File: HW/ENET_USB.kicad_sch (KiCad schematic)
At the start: 0 parts

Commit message: USB hub, connector, load switch
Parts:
- added C? (x2): 100uF, Capacitor_SMD:CP_Elec_6.3x5.8, symbol Device:C_Polarized_US
- added C? (x3): 0.1u, Capacitor_SMD:C_0603_1608Metric, symbol Device:C
- added C? (x3): 22uF, Capacitor_SMD:C_1210_3225Metric, symbol Device:C
- added C? (x2): 1u, Capacitor_SMD:C_0603_1608Metric, symbol Device:C
- added C? (x2): 18pF, Capacitor_SMD:C_0603_1608Metric, symbol Device:C
- added J?: UJ2-ADH-1-TH, symbol KlipperShip_Symbols:UJ2-ADH-1-TH
- added R?: 0R, Resistor_SMD:R_0603_1608Metric, symbol Device:R_US
- added R?: 12k 1%, Resistor_SMD:R_0603_1608Metric, symbol Device:R_US
- added U?: USB2422, Package_DFN_QFN:QFN-24-1EP_4x4mm_P0.5mm_EP2.6x2.6mm, symbol KlipperShip_Symbols:USB2422
- added U?: TPS2042D, Package_SO:SOIC-8_3.9x4.9mm_P1.27mm, symbol Power_Management:TPS2042D
- added Y?: 24MHz, Crystal:Crystal_SMD_3225-4Pin_3.2x2.5mm, symbol Device:Crystal_GND24
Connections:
- new net +3V3: C?.1, C?.1, C?.1, R?.1, U?.1 (VDD33), U?.18 (VDD33), U?.9 (VDD33)
- new net +5V: C?.1, U?.2 (IN1)
- new net GND: C?.2, C?.2, C?.2, C?.2, C?.2, C?.2, C?.2, C?.2, C?.2, C?.2, C?.2, C?.2, J?.4 (GND), J?.8 (GND), R?.2, U?.1 (GND), U?.25 (PAD), Y?.2, Y?.4
- new net I2C_USB_SCL: U?.14 (SCL)
- new net I2C_USB_SDA: U?.13 (SDA)
- new net USB_CM_DN: U?.19 (USB_UP_DM)
- new net USB_CM_DP: U?.20 (USB_UP_DP)
- new net USB_DS1_DM: J?.2 (DM1), U?.2 (USB_DS1_DM)
- new net USB_DS1_DP: J?.3 (DP1), U?.3 (USB_DS1_DP)
- new net USB_DS2_DM: J?.6 (DM2), U?.4 (USB_DS2_DM)
- new net USB_DS2_DP: J?.7 (DP2), U?.5 (USB_DS2_DP)
- new net USB_RBIAS: R?.1, U?.24 (RBIAS)
- new net USB_RST: U?.15 (RST_N)
- new net USB_VBUS_DIV: R?.2, U?.16 (VBUS_DET)
- new net USB_VDD_CAP: C?.1, U?.10 (VDD_CAP)
- new net USB_VDD_PLL: C?.1, U?.23 (VDD_PLL)
- new net USB_XTAL_N: U?.21 (XTALOUT)
- new net USB_XTAL_P: C?.1, U?.22 (XTALIN), Y?.1
- new net UXB_XTAL_N: C?.1, Y?.3
- new net VBUS1: C?.1, C?.1, J?.1 (VCC1), U?.7 (OUT1)
- new net VBUS2: C?.1, C?.1, J?.5 (VCC2), U?.6 (OUT2)
- no-connect marks 0 -> 1
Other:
- note added: "PIN 1"
- note added: "PIN 18"
- note added: "PIN 9"

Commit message: More work on USB, added Enet jack
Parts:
- removed U?: TPS2042D, Package_SO:SOIC-8_3.9x4.9mm_P1.27mm, symbol Power_Management:TPS2042D
- added C? (x2): 0.1u, Capacitor_SMD:C_0603_1608Metric, symbol Device:C
- added J?: RJ45_Amphenol_RJMG1BD3B8K1ANR, Connector_RJ:RJ45_Amphenol_RJMG1BD3B8K1ANR, symbol Connector:RJ45_Amphenol_RJMG1BD3B8K1ANR
- added R? (x3): 0R, Resistor_SMD:R_0603_1608Metric, symbol Device:R_US
- added R? (x4): 10k 1%, Resistor_SMD:R_0603_1608Metric, symbol Device:R_US
- added R? (x2): 100R, Resistor_SMD:R_0603_1608Metric, symbol Device:R_US
- added U?: TPS2052BDR, Package_SO:SOIC-8_3.9x4.9mm_P1.27mm, symbol KlipperShip_Symbols:TPS2052BDR
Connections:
- net +3V3: now also J?.L1 (LEDY_A), J?.L4 (LEDG_A), R?.1, R?.1
- net +5V: now also U?.2 (IN1)
- net GND: now also C?.2, C?.2, J?.R8 (GND), R?.2, R?.2, U?.1 (GND)
- net I2C_USB_SCL: now also R?.2
- net I2C_USB_SDA: now also R?.2
- net USB_RST: now also R?.2
- net VBUS1: now also U?.7 (OUT1)
- net VBUS2: now also U?.6 (OUT2)
- net USB_DS2_PEN: now reaches U?.11 (PRTPWR2)
- net USB_DS2_PEN: now also R?.1, U?.4 (~EN2)
- net USB_DS2_OCR: now reaches U?.12 (OCR2_N)
- net USB_DS2_OCR: now also R?.2, U?.5 (~OC2)
- net USB_DS1_PEN: now reaches U?.7 (PRTPWR1)
- net USB_DS1_PEN: now also R?.1, U?.3 (~EN1)
- net USB_DS1_OCR: now reaches U?.8 (OCR1_N)
- net USB_DS1_OCR: now also R?.2, U?.8 (~OC1)
- net Earth: now reaches J?.10 (SHLD2)
- net Earth: now also J?.11 (SHLD3), J?.12 (SHLD4), J?.9 (SHLD1), J?.13 (SHIELD)
- new net ETH_LEDR_G: J?.L3 (LEDG_K), R?.2
- new net ETH_LEDR_Y: J?.L2 (LEDY_K), R?.2
- new net ETH_LED_G: R?.1
- new net ETH_LED_Y: R?.1
- new net TRD0_CT: C?.1, J?.R4 (TCT)
- new net TRD0_N: J?.R2 (TD-)
- new net TRD0_P: J?.R1 (TD+)
- new net TRD1_CT: C?.1, J?.R5 (RCT)
- new net TRD1_N: J?.R6 (RD-)
- new net TRD1_P: J?.R3 (RD+)
- new net USB_SOM_RST: R?.1
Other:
- moved on the sheet: C?, Y?

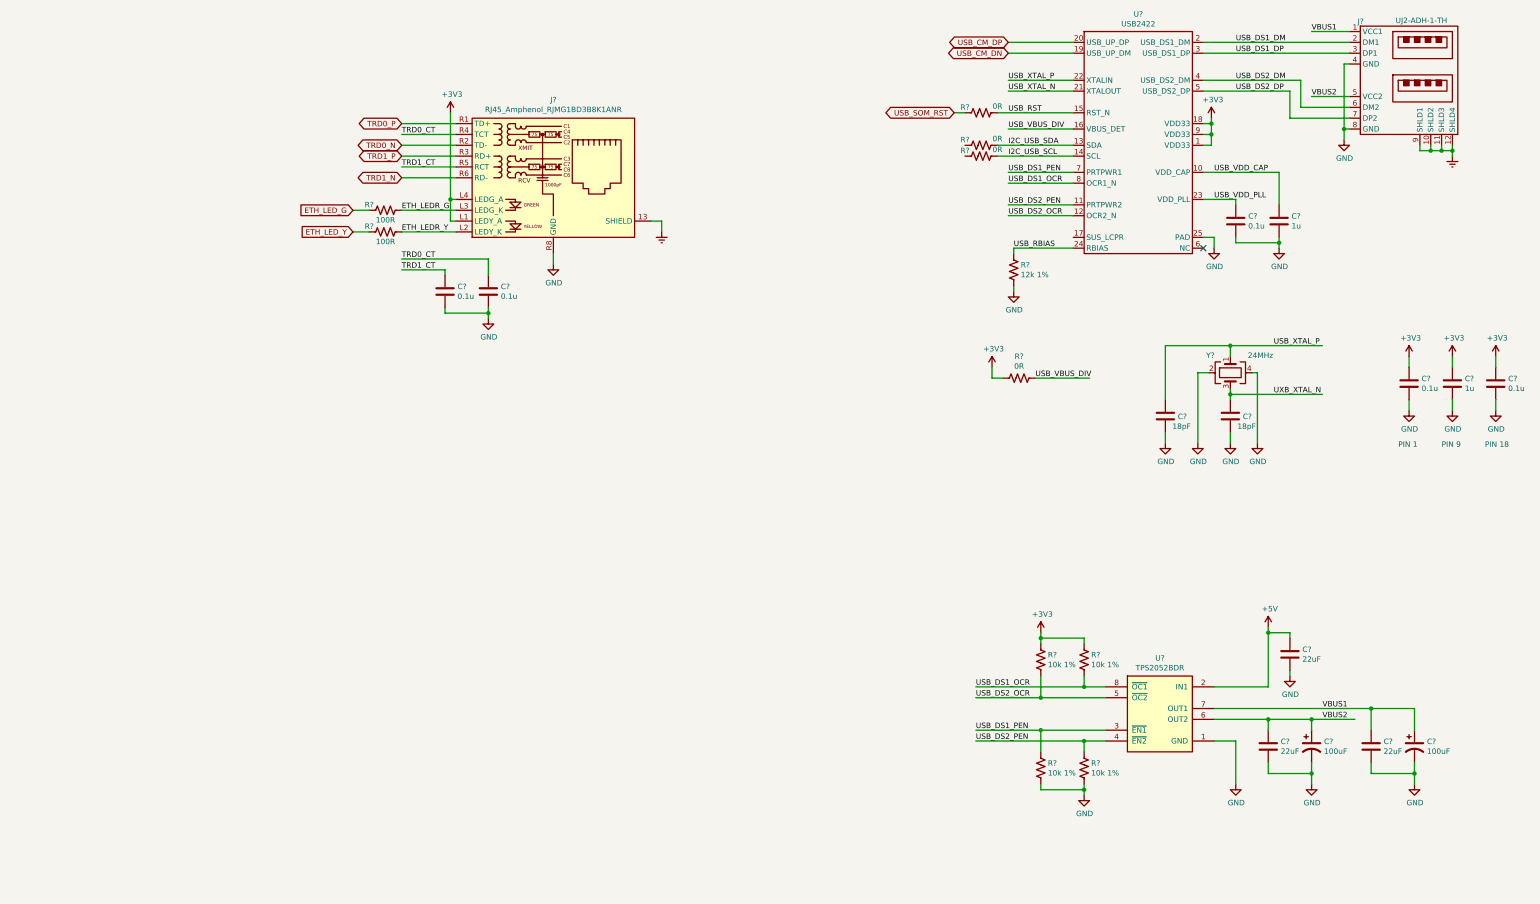
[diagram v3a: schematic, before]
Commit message: Added first pieces of SD card connector for SOM, USB TVS
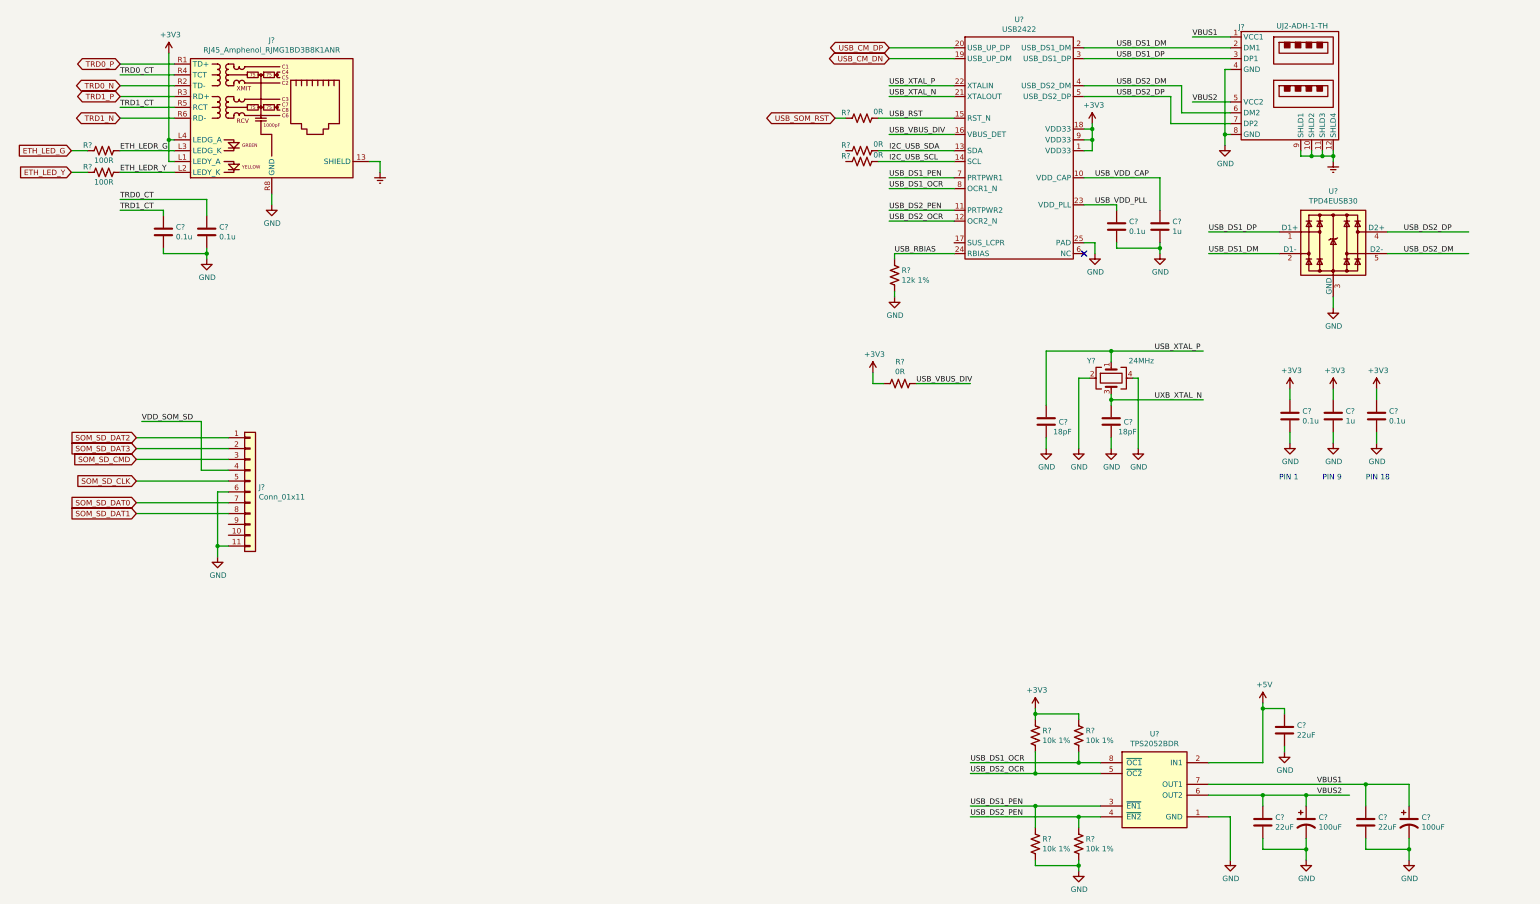
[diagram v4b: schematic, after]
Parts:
- added J?: Conn_01x11, Connector_Card:microSD_HC_Hirose_DM3AT-SF-PEJM5, symbol Connector_Generic:Conn_01x11
- added U?: TPD4EUSB30, Package_SON:USON-10_2.5x1.0mm_P0.5mm, symbol Power_Protection:TPD4EUSB30
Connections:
- net GND: now also J?.11 (Pin_11), J?.6 (Pin_6), U?.3 (GND), U?.8 (GND)
- net USB_DS1_DM: now also U?.2 (D1-)
- net USB_DS1_DP: now also U?.1 (D1+)
- net USB_DS2_DM: now also U?.5 (D2-)
- net USB_DS2_DP: now also U?.4 (D2+)
- new net SOM_SD_CLK: J?.5 (Pin_5)
- new net SOM_SD_CMD: J?.3 (Pin_3)
- new net SOM_SD_DAT0: J?.7 (Pin_7)
- new net SOM_SD_DAT1: J?.8 (Pin_8)
- new net SOM_SD_DAT2: J?.1 (Pin_1)
- new net SOM_SD_DAT3: J?.2 (Pin_2)
- new net VDD_SOM_SD: J?.4 (Pin_4)
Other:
- moved on the sheet: C?, J?, R?, U?, Y?
